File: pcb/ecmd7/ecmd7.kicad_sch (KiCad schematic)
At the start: 109 parts, among them J1 PMOD_SPI_ENC, J10 SPI Ext., J2 PMOD_ADC_MPIO, J3 PMOD_DRV, J4 Conn_01x02_Socket, J5 Encoder, J6 12V, J7 RS422/BISS-C, J8 5V, J9 FH35C-19S-0.3SHW_99_, Q1 IRFS3806, Q11 MMBT3904, Q12 MMBT3904, Q2 IRFS3806, Q3 IRFS3806, Q4 IRFS3806, Q5 IRFS3806, Q6 IRFS3806, U1 TMC6200-TA, U15 74LVC1G139, U16 MB85RS1MT, X1 EA W096016-XBLW

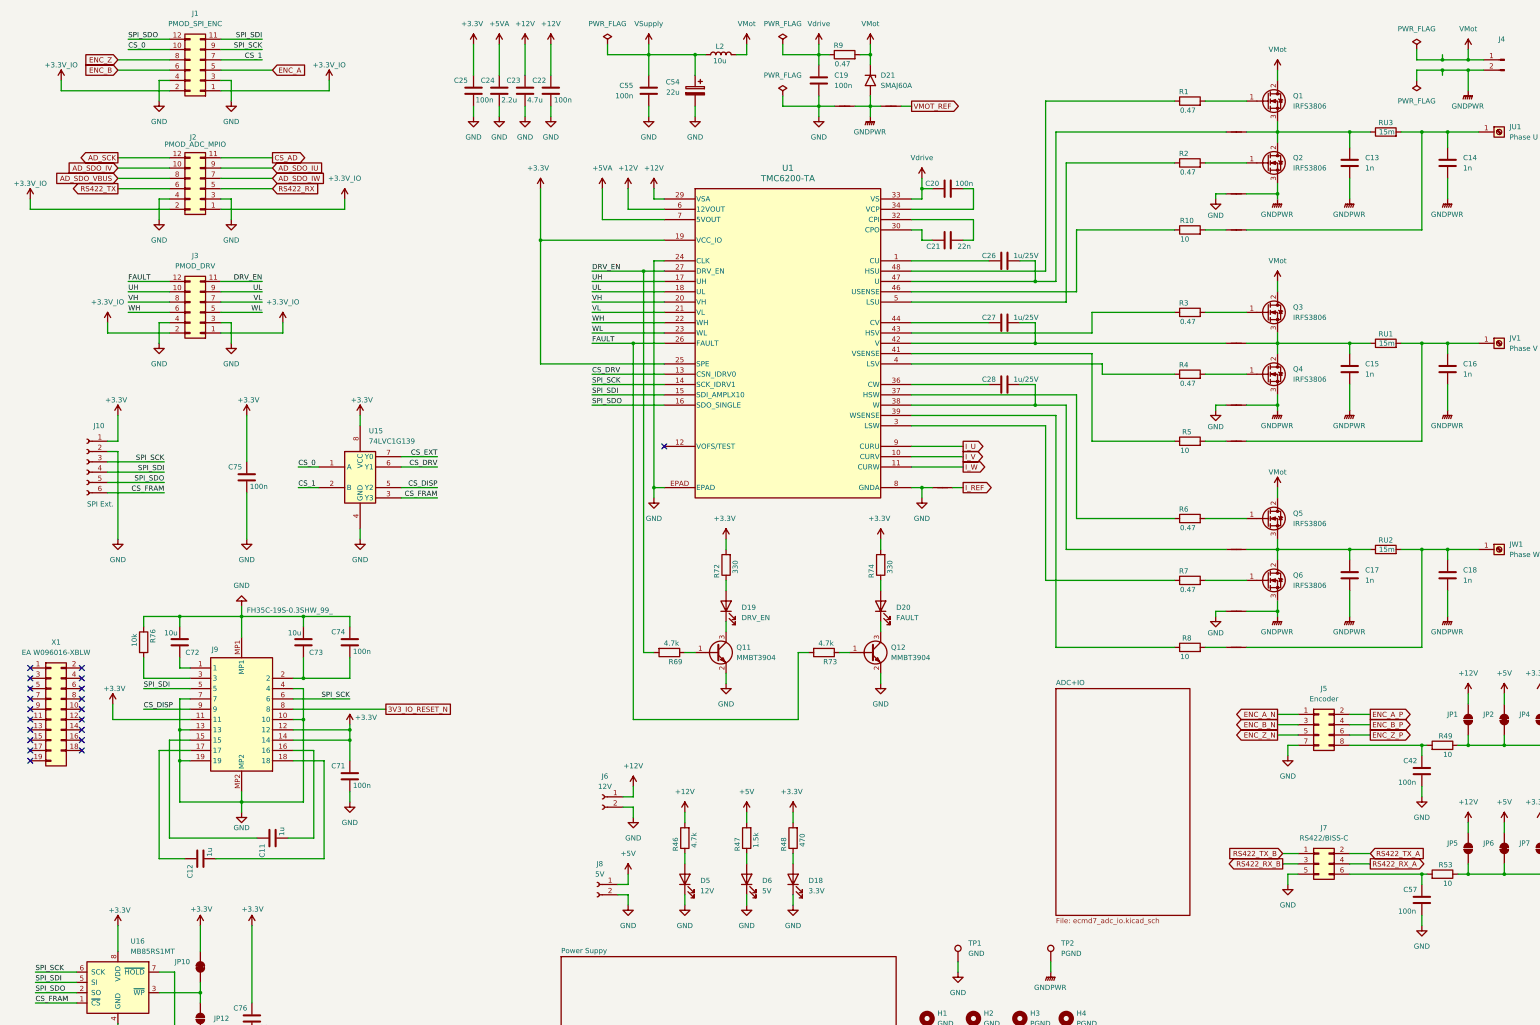
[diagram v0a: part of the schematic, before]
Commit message: WIP: Partial routing
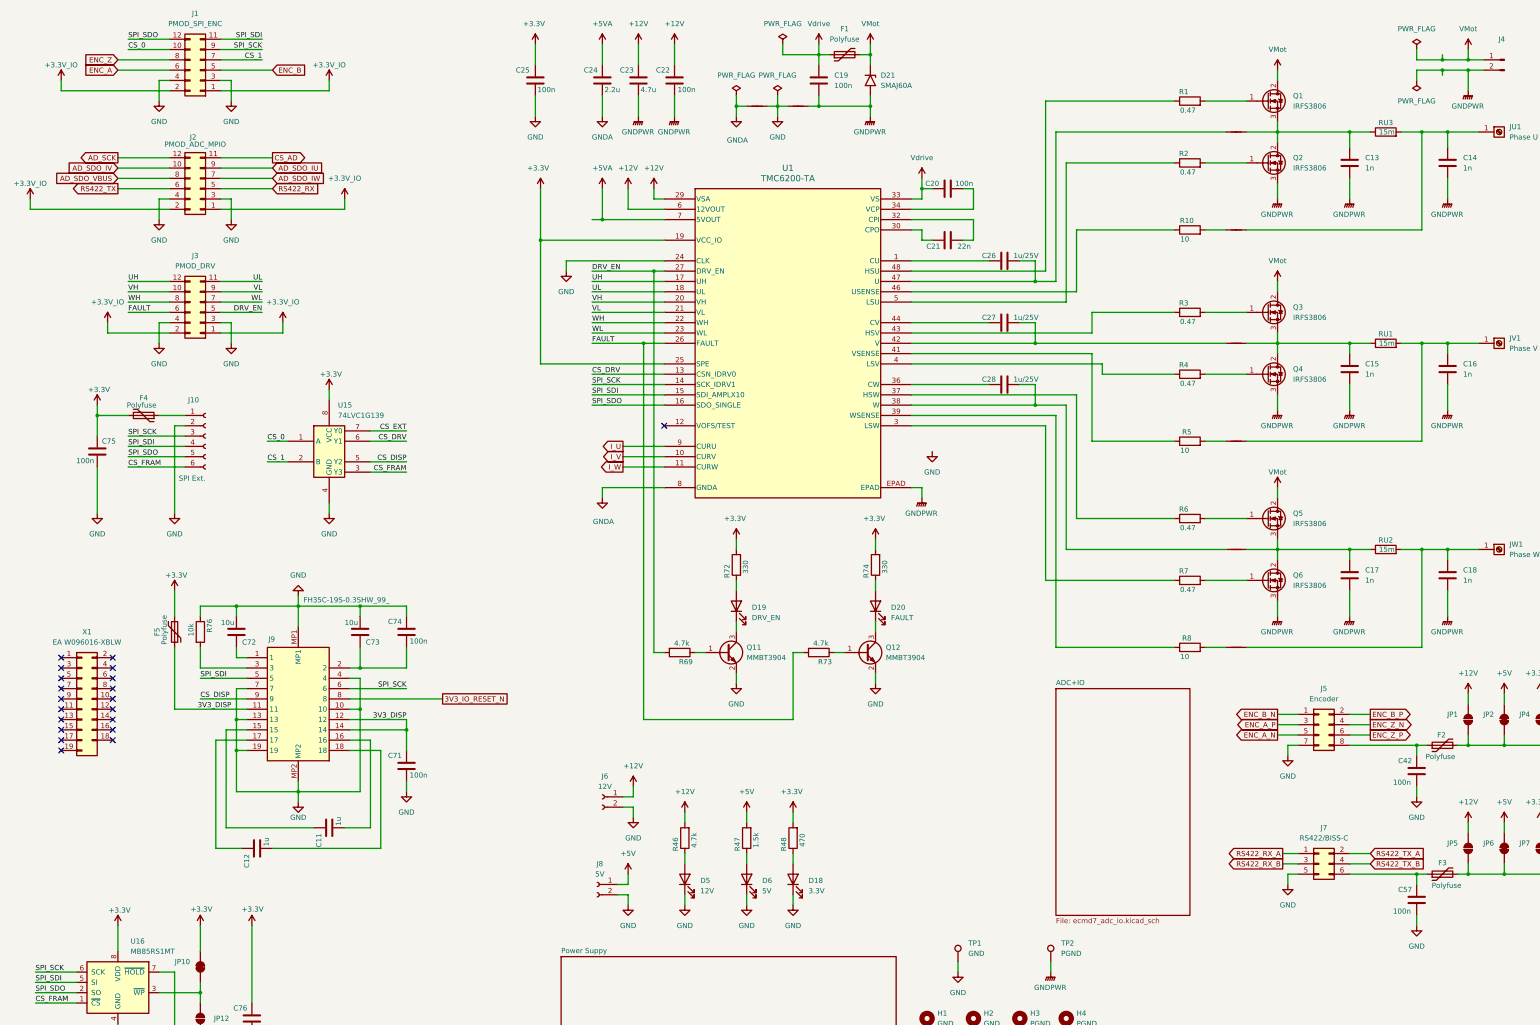
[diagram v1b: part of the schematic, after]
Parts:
- removed C54: 22u, Capacitor_SMD:CP_Elec_6.3x9.9, symbol Device:C_Polarized
- removed C55: 100n, Capacitor_SMD:C_0805_2012Metric, symbol Device:C
- removed L2: 10u, Inductor_SMD:L_TechFuse_SL0530, symbol Device:L
- removed NTGU1, NTGV1, NTGW1, NTPV2, NTPW3: NetTie_2, NetTie:NetTie-2_SMD_Pad0.5mm, symbol Device:NetTie_2
- removed R49, R53: 10, Resistor_SMD:R_0805_2012Metric, symbol Device:R
- removed R9: 0.47, Resistor_SMD:R_0805_2012Metric, symbol Device:R
- added F1, F2, F3, F4, F5: Polyfuse, Fuse:Fuse_0805_2012Metric, symbol Device:Polyfuse
- added NTP2G2: NetTie_2, NetTie:NetTie-2_SMD_Pad0.5mm, symbol Device:NetTie_2
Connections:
- net +3.3V: now also F4.2, F5.2; no longer C71.1, J10.1 (Pin_1), J9.11, J9.12, J9.14
- net DRV_EN: now also J3.5 (Pin_5); no longer J3.11 (Pin_11)
- net ENC_A: now also J1.6 (Pin_6); no longer J1.5 (Pin_5)
- net ENC_A_N: now also J5.5 (Pin_5); no longer J5.1 (Pin_1)
- net ENC_A_P: now also J5.3 (Pin_3); no longer J5.2 (Pin_2)
- net ENC_B: now also J1.5 (Pin_5); no longer J1.6 (Pin_6)
- net ENC_B_N: now also J5.1 (Pin_1); no longer J5.3 (Pin_3)
- net ENC_B_P: now also J5.2 (Pin_2); no longer J5.4 (Pin_4)
- net ENC_Z_N: now also J5.4 (Pin_4); no longer J5.5 (Pin_5)
- net FAULT: now also J3.6 (Pin_6); no longer J3.12 (Pin_12)
- net GND: now also NTP2G2.1; no longer C19.2, C22.2, C23.2, C24.2, U1.8 (GNDA), U1.EPAD
- net GNDPWR: now also C19.2, C22.2, C23.2, U1.EPAD
- net RS422_RX_A: now also J7.1 (Pin_1); no longer J7.4 (Pin_4)
- net RS422_TX_B: now also J7.4 (Pin_4); no longer J7.1 (Pin_1)
- net UH: now also J3.12 (Pin_12); no longer J3.10 (Pin_10)
- net UL: now also J3.11 (Pin_11); no longer J3.9 (Pin_9)
- net VH: now also J3.10 (Pin_10); no longer J3.8 (Pin_8)
- net VL: now also J3.9 (Pin_9); no longer J3.7 (Pin_7)
- net VMot: now also F1.2
- net Vdrive: now also F1.1
- net WH: now also J3.8 (Pin_8); no longer J3.6 (Pin_6)
- net WL: now also J3.7 (Pin_7); no longer J3.5 (Pin_5)
- net at C57.1, J7.6 (Pin_6): now also F3.1
- net at JP5.1 (A), JP6.1 (A), JP7.1 (A): now also F3.2
- net at C42.1, J5.8 (Pin_8): now also F2.1
- net at JP1.1 (A), JP2.1 (A), JP4.1 (A): now also F2.2
- new net: F4.1, J10.1 (Pin_1)
- new net 3V3_DISP: C71.1, F5.1, J9.11, J9.12, J9.14
- new net GNDA: C24.2, NTP2G2.2, U1.8 (GNDA)
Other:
- moved on the sheet: C11, C12, C22, C23, C24, C25, C42, C57, C71, C72, C73, C74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

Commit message: WIP: advnced  routing
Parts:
- added TP3: U, TestPoint:TestPoint_Loop_D2.50mm_Drill1.0mm, symbol Connector:TestPoint
- added TP4: V, TestPoint:TestPoint_Loop_D2.50mm_Drill1.0mm, symbol Connector:TestPoint
- added TP5: W, TestPoint:TestPoint_Loop_D2.50mm_Drill1.0mm, symbol Connector:TestPoint
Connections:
- net CS_EXT: now also J10.6 (Pin_6)
- net CS_FRAM: no longer J10.6 (Pin_6)
- net at C14.1, JU1.1 (Pin_1), NTSU1.1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: now also TP3.1
- net at C18.1, JW1.1 (Pin_1), NTSW1.2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: now also TP5.1
- net at C16.1, JV1.1 (Pin_1), NTSV1.2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: now also TP4.1
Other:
- note added: "OLED Display"
- moved on the sheet: C11, C12, C71, C72, C73, C74, C75, C76, D18, D5, D6, F4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

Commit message: Routing complete, DRC successful
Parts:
- removed C11, C12: 1u, Capacitor_SMD:C_0805_2012Metric, symbol Device:C
- removed C71, C74, C75, C76: 100n, Capacitor_SMD:C_0805_2012Metric, symbol Device:C
- removed C72, C73: 10u, Capacitor_SMD:C_0805_2012Metric, symbol Device:C
- removed F4, F5: Polyfuse, Fuse:Fuse_0805_2012Metric, symbol Device:Polyfuse
- removed J10: SPI Ext., Connector_PinSocket_2.54mm:PinSocket_1x06_P2.54mm_Vertical, symbol Connector:Conn_01x06_Socket
- removed J9: FH35C-19S-0.3SHW_99_, SSTA:FH35C19S03SHW99, symbol SSTA:FH35C-19S-0.3SHW_99_
- removed JP10: SolderJumper_2_Bridged, Jumper:SolderJumper-2_P1.3mm_Bridged_RoundedPad1.0x1.5mm, symbol Jumper:SolderJumper_2_Bridged
- removed JP12: SolderJumper_2_Open, Jumper:SolderJumper-2_P1.3mm_Open_RoundedPad1.0x1.5mm, symbol Jumper:SolderJumper_2_Open
- removed R76: 10k, Resistor_SMD:R_0805_2012Metric, symbol Device:R
- removed U15: 74LVC1G139, Package_SO:SSOP-8_2.95x2.8mm_P0.65mm, symbol 74xGxx:74LVC1G139
- removed U16: MB85RS1MT, Package_SO:SOP-8_3.76x4.96mm_P1.27mm, symbol Memory_NVRAM:MB85RS1MT
- removed X1: EA W096016-XBLW, symbol Connector_Generic:Conn_2Rows-19Pins
- added NTP2G4: NetTie_2, NetTie:NetTie-2_SMD_Pad2.0mm, symbol Device:NetTie_2
- renumbered RU3 to RU1, RU1 to RV1, RU2 to RW1, TP3 to TPU1, TP4 to TPV1, TP5 to TPW1
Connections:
- net CS_0 renamed CS0
- net CS_1 renamed CS1
- net CS_AD renamed ~{CS_AD}
- net CS_DRV renamed ~{CS_DRV}
- net GNDPWR renamed GNDMOT
- net GNDMOT: now also NTP2G4.1; no longer C19.2, C22.2, C23.2, NTP2G1.1, U1.EPAD
- net Vdrive renamed VDrv
- new net GNDDRV: C19.2, C22.2, C23.2, NTP2G1.1, NTP2G4.2, U1.EPAD
- no-connect marks 20 -> 1
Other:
- note removed: "OLED Display"
- moved on the sheet: C19, D21, F1, R1, R2, R3, R4, R6, R7

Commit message: Final layout
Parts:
- added H5: VMOT, MountingHole:MountingHole_3.2mm_M3_Pad_Via, symbol Mechanical:MountingHole_Pad
- C23: value 4.7u -> 4.7u/25V
- C24: value 2.2u -> 2.2u/25V
- J6, J8: footprint Connector_PinHeader_2.54mm:PinHeader_1x02_P2.54mm_Vertical -> Connector_PinSocket_2.54mm:PinSocket_1x02_P2.54mm_Vertical
- JP1, JP5: value SolderJumper_2_Open -> 12V
- JP2, JP6: value SolderJumper_2_Bridged -> 5V
- JP4, JP7: value SolderJumper_2_Open -> 3V3
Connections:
- net VMot: now also H5.1
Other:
- moved on the sheet: C22, C24
